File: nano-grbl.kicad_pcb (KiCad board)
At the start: 2 copper layers, 100 x 50 mm, 21 parts, among them J1 System Control, J2 5V, J3 3.3V, J4 12V Power In, J5 Stepper Driver, J6 Serial, J7 X Limit, J8 Y Limit, J9 Z Limit, U1 LTV-817S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

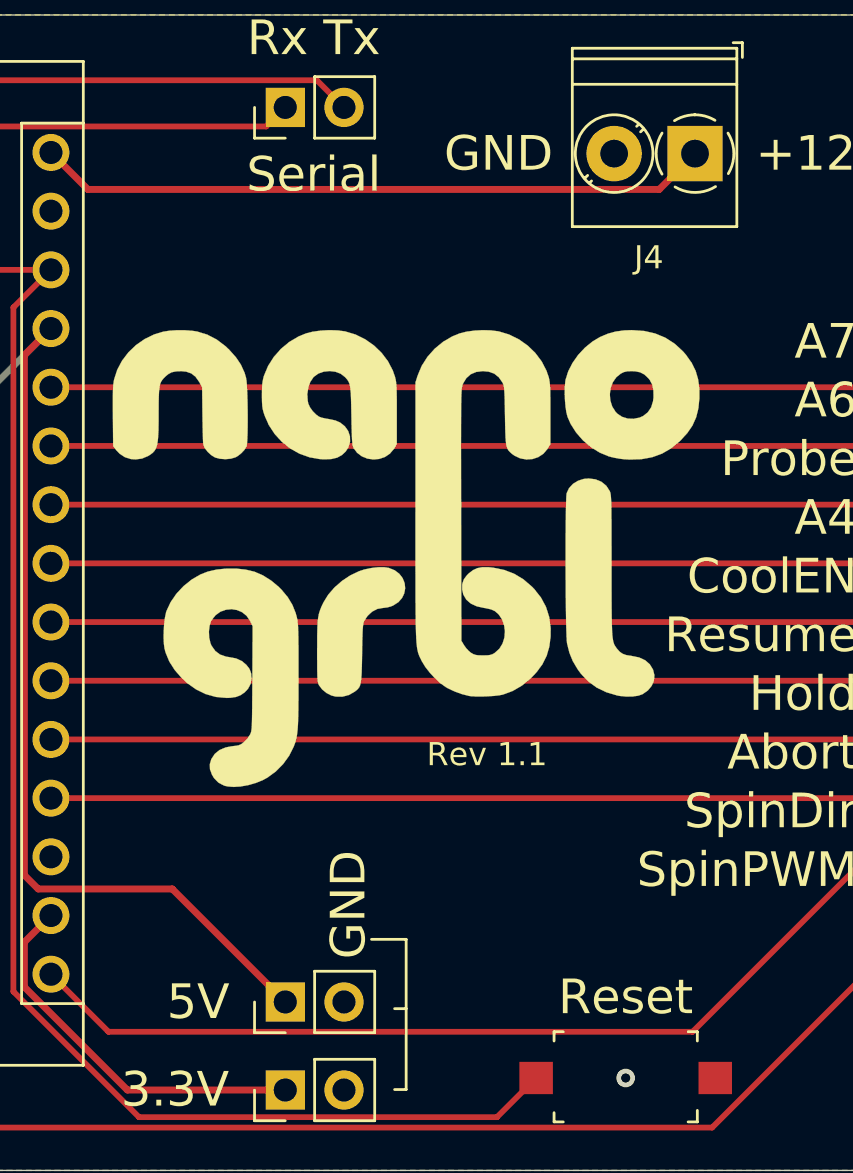
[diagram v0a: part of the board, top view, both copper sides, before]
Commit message: Update README and pcb for new footprint location.
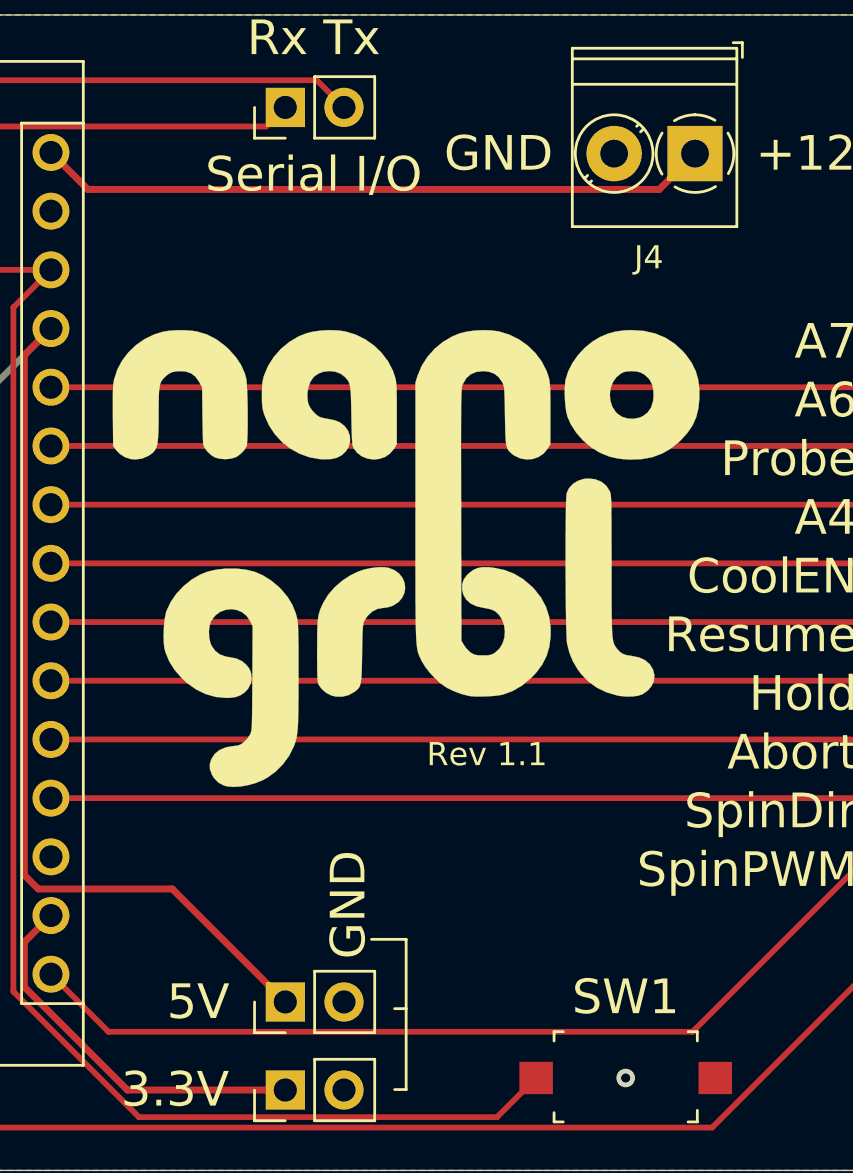
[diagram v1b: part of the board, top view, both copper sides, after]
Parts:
- J6: value Serial -> Serial I/O
- renumbered Reset to SW1
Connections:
- A1 pad 18: (no net) -> Net-(A1-Pad18)
